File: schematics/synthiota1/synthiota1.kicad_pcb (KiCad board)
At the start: 2 copper layers, 177.8 x 114.3 mm, 111 parts, among them IC1 H11L1, J1 PJ-320A-4P DIP, J2 PJ-320A-4P DIP, SW1 SW_Push, SW2 SW_Push, SW3 SW_Push, U1 Pico, U2 74HC4051, U3 MPR121QR2, U4 MPR121QR2

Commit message: pcb cleanup
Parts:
- moved C25 8.53 mm to (179.9, 49.6)
- moved C26 8.53 mm to (163.1, 49.6)
- moved LED25 8.53 mm to (140.9, 48.9)
- moved LED26 8.53 mm to (155.9, 48.9)
- moved LED27 8.53 mm to (170.9, 48.9)
- moved SW1 8.53 mm to (167.7, 39.6)
- moved SW2 8.53 mm to (137.7, 39.6)
- moved SW3 8.53 mm to (152.7, 39.6)
- moved C27 8.52 mm to (148.3, 49.6)
- moved SLIDER2 1.13 mm to (132.5, 77.9)
- moved SLIDER1 0.87 mm to (30.5, 78.1)
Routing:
- net +VLED: track 947.3 -> 937.9 mm
- net /SWA: track 124.4 -> 132.9 mm
- net Net-(LED24-DOUT): track 86.4 -> 78.2 mm
- net /SWB: track 104.2 -> 112.3 mm
- net /SWC: track 116.1 -> 124.1 mm
- net Net-(U4-ELE2): track 78.9 -> 81.0 mm
- net Net-(U4-ELE0): track 30.7 -> 32.5 mm
- net Net-(U4-ELE1): track 56.2 -> 54.9 mm
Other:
- board text added: "PJ320A"
- board text added: "prototype"

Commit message: pcb cleanup
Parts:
- added C33: 100n, Capacitor_SMD:C_0603_1608Metric, B.Cu at (97.4, 43.0)
- added MODULE2: ~, todbot_eagle2023:I2S_PCM_5100_SOUNDCARD, F.Cu at (157.2, 33.5)
- MODULE1: value ~ -> Pico; footprint todbot_eagle2023:I2S_PCM_5100_SOUNDCARD -> todbot_RPI_Pico:RPi_Pico_SMD_TH
- U1: value Pico -> H11L1; footprint todbot_RPI_Pico:RPi_Pico_SMD_TH -> easyeda2kicad:SMD-6_L7.3-W6.5-P2.54-LS10.2-BL; moved to B.Cu
- moved MODULE1 113.0 mm to (44.2, 33.3), turned to 90 degrees
- moved U1 62.3 mm to (106.4, 31.0), turned to -90 degrees
- moved C25 32.0 mm to (147.9, 49.6)
- moved C27 31.6 mm to (179.9, 49.6)
- moved R23 2.30 mm to (27.9, 69.8)
- moved R22 2.20 mm to (23.4, 69.8)
- renumbered C100 to C28, C104 to C29, C103 to C30, C101 to C31, C102 to C32, D100 to D1, R17 to R1, R18 to R2, R20 to R3, R19 to R4, R24 to R5, R21 to R6, IC1 to U1
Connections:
- D1 pad 1: Net-(D100-K) -> Net-(D1-K)
- D1 pad 2: Net-(D100-A) -> Net-(D1-A)
- J2 pad D: Net-(D100-A) -> Net-(D1-A)
- MODULE1 pad 3: unconnected-(MODULE1-Pad3) -> GND
- MODULE1 pad 4: unconnected-(MODULE1-Pad4) -> /SDA
- MODULE1 pad 5: unconnected-(MODULE1-Pad5) -> /SCL
- R3 pad 2: Net-(D100-K) -> Net-(D1-K)
- U1 pad 1: Net-(D100-K) -> Net-(D1-K)
- U1 pad 2: Net-(D100-A) -> Net-(D1-A)
- U1 pad 3: unconnected-(IC1-Pad3) -> unconnected-(U1-Pad3)
- U1 pad 1: unconnected-(U1-GPIO0-Pad1) -> Net-(D1-K)
- U1 pad 2: unconnected-(U1-GPIO1-Pad2)_1 -> Net-(D1-A)
- U1 pad 3: GND -> unconnected-(U1-Pad3)
- U1 pad 4: /SDA -> /MIDI_IN
- U1 pad 5: /SCL -> GND
- U1 pad 6: unconnected-(U1-GPIO4-Pad6) -> +3V3
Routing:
- net Net-(D100-A): track 31.4 -> 0.00 mm
- net Net-(D1-A): track 0.00 -> 31.4 mm
- net Net-(D100-K): track 14.7 -> 0.00 mm
- net Net-(D1-K): track 0.00 -> 14.7 mm
- net +VLED: track 937.9 -> 950.7 mm
- net /SDA: track 155.1 -> 151.8 mm
- net /SCL: track 153.9 -> 151.0 mm
- net Net-(LED16-DOUT): track 231.3 -> 230.2 mm
- net +3V3: track 453.2 -> 453.8 mm
- net /LEDDAT: track 130.3 -> 130.8 mm
- net GND: vias 3 -> 5
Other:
- board text added: "3V3"
- board text added: "VLED"
- board text added: "VSYS"

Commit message: pcb tweaks
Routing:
- net Net-(LED16-DOUT): track 230.2 -> 229.3 mm
- net +VLED: track 950.7 -> 949.8 mm
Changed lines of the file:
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@@
 	)
 	(via
-		(at 25.6 83.6)
+		(at 150.325 49.6)
 		(size 0.6)
 		(drill 0.3)
 		(layers "F.Cu" "B.Cu")
-		(free yes)
 		(net 3)
 	)
 	(via
-		(at 150.325 49.6)
+		(at 23.4 81.4)
 		(size 0.6)
 		(drill 0.3)
 		(layers "F.Cu" "B.Cu")
+		(free yes)
 		(net 3)
 	)
 	(via
-		(at 23.4 81.4)
+		(at 25 84)
 		(size 0.6)
 		(drill 0.3)
@@
 	)
 	(segment
-		(start 22.4 105.2)
-		(end 18.162 100.962)
-		(width 0.5)
-		(layer "B.Cu")
-		(net 57)
-	)
-	(segment
 		(start 175.925 49.65)
 		(end 179.1 49.65)
@@
 	)
 	(segment
-		(start 27.56 30.16)
-		(end 27.56 27.846)
-		(width 0.5)
-		(layer "B.Cu")
-		(net 57)
-	)
-	(segment
 		(start 139.125 105.125)
 		(end 139.125 97.25)
@@
 	)
 	(segment
-		(start 34.65 36.95)
-		(end 34.65 32.65)
-		(width 0.5)
-		(layer "B.Cu")
-		(net 57)
-	)
-	(segment
 		(start 145.725 49.6)
 		(end 145.675 49.65)
@@
 	)
 	(segment
+		(start 23.8 105.2)
+		(end 18.162 99.562)
+		(width 0.5)
+		(layer "B.Cu")
+		(net 57)
+	)
+	(segment
 		(start 145.725 49.6)
 		(end 147.55 49.6)
@@
 	)
 	(segment
+		(start 34.65 36.95)
+		(end 34.65 32.65)
+		(width 0.5)
+		(layer "B.Cu")
+		(net 57)
+	)
+	(segment
 		(start 184.375 74.15)
 		(end 184.625 74.4)
@@
 	)
 	(segment
+		(start 33.086 38.514)
+		(end 34.65 36.95)
+		(width 0.5)
+		(layer "B.Cu")
+		(net 57)
+	)
+	(segment
 		(start 79.125 117.25)
 		(end 82.375 117.25)
@@
 	)
 	(segment
-		(start 18.162 100.962)
+		(start 18.162 99.562)
 		(end 18.162 40.292)
 		(width 0.5)
@@
 	)
 	(segment
-		(start 33 31)
-		(end 28.4 31)
-		(width 0.5)
-		(layer "B.Cu")
-		(net 57)
-	)
-	(segment
 		(start 79.125 104.2)
 		(end 79.125 97.25)
@@
 	)
 	(segment
+		(start 34.65 32.65)
+		(end 33 31)
+		(width 0.5)
+		(layer "B.Cu")
+		(net 57)
+	)
+	(segment
 		(start 162.375 117.25)
 		(end 163.025 117.9)
@@
 	)
 	(segment
+		(start 18.162 40.292)
+		(end 19.94 38.514)
+		(width 0.5)
+		(layer "B.Cu")
+		(net 57)
+	)
+	(segment
 		(start 160.125 76.525)
 		(end 160.2 76.6)
@@
 	)
 	(segment
-		(start 18.162 40.292)
-		(end 19.94 38.514)
-		(width 0.5)
+		(start 159.125 105.125)
+		(end 159.125 97.25)
+		(width 0.3048)
 		(layer "B.Cu")
 		(net 57)
 	)
 	(segment
-		(start 34.65 32.65)
-		(end 33 31)
+		(start 28.4 31)
+		(end 27.56 30.16)
 		(width 0.5)
 		(layer "B.Cu")
@@
 	)
 	(segment
-		(start 159.125 105.125)
-		(end 159.125 97.25)
-		(width 0.3048)
-		(layer "B.Cu")
-		(net 57)
-	)
-	(segment
 		(start 23.8 105.2)
 		(end 23.8 122.8)
@@
 	)
 	(segment
-		(start 19.94 38.514)
-		(end 33.086 38.514)
-		(width 0.5)
-		(layer "B.Cu")
-		(net 57)
-	)
-	(segment
 		(start 99.9 104.3)
 		(end 99.125 103.525)
@@
 	)
 	(segment
-		(start 28.4 31)
-		(end 27.56 30.16)
-		(width 0.5)
-		(layer "B.Cu")
-		(net 57)
-	)
-	(segment
 		(start 159.125 97.25)
 		(end 162.375 97.25)
@@
 	)
 	(segment
+		(start 27.56 30.16)
+		(end 27.56 27.846)
+		(width 0.5)
+		(layer "B.Cu")
+		(net 57)
+	)
+	(segment
 		(start 163.025 125.625)
 		(end 163.2 125.8)
@@
 	)
 	(segment
-		(start 33.086 38.514)
-		(end 34.65 36.95)
+		(start 19.94 38.514)
+		(end 33.086 38.514)
 		(width 0.5)
 		(layer "B.Cu")
@@
 	)
 	(segment
-		(start 23.8 105.2)
-		(end 22.4 105.2)
+		(start 33 31)
+		(end 28.4 31)
 		(width 0.5)
 		(layer "B.Cu")
@@
 	)
 	(segment
-		(start 29.2 74.15)
-		(end 29.05 74.15)
+		(start 21.6 81.6)
+		(end 21.6 106.8)
 		(width 0.3048)
 		(layer "F.Cu")
@@
 	)
 	(segment
-		(start 21 82.2)
-		(end 21 107)
+		(start 21.6 106.8)
+		(end 22.8 108)
 		(width 0.3048)
 		(layer "F.Cu")
@@
 	)
 	(segment
-		(start 22 108)
-		(end 188.8 108)
+		(start 29.2 74.15)
+		(end 29.05 74.15)
 		(width 0.3048)
 		(layer "F.Cu")
@@
 	)
 	(segment
-		(start 21 107)
-		(end 22 108)
+		(start 29.05 74.15)
+		(end 21.6 81.6)
 		(width 0.3048)
 		(layer "F.Cu")
@@
 	)
 	(segment
-		(start 29.05 74.15)
-		(end 21 82.2)
+		(start 22.8 108)
+		(end 188.8 108)
 		(width 0.3048)
 		(layer "F.Cu")

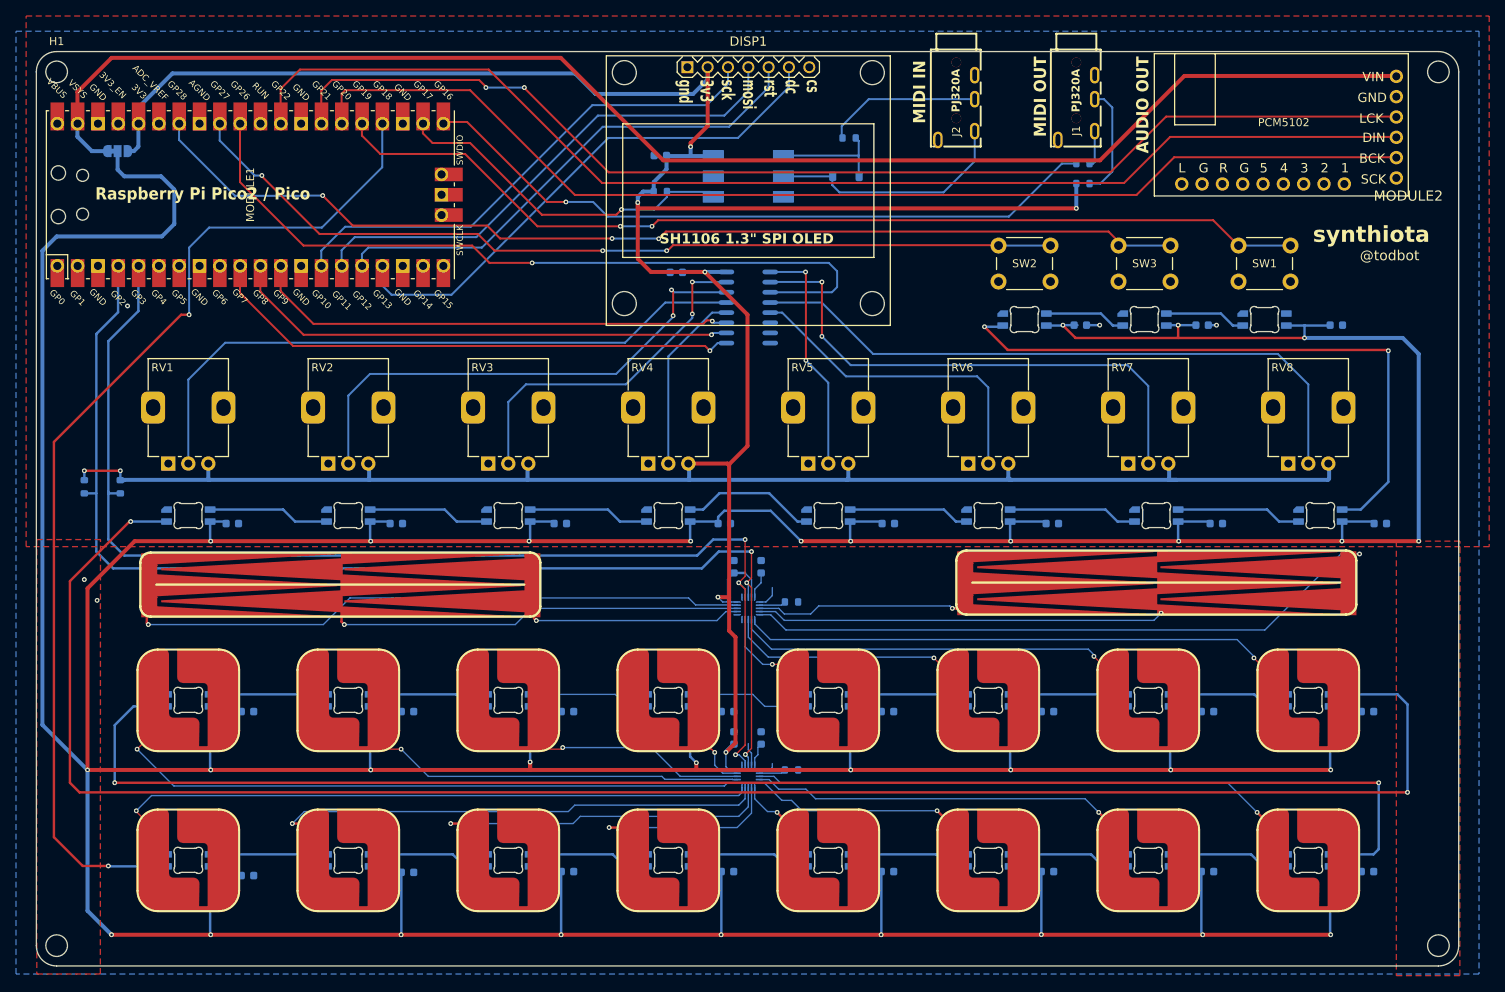
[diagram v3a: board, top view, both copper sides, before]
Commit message: lcsc part nums for everything because jlc sucks now, pcb cleanup
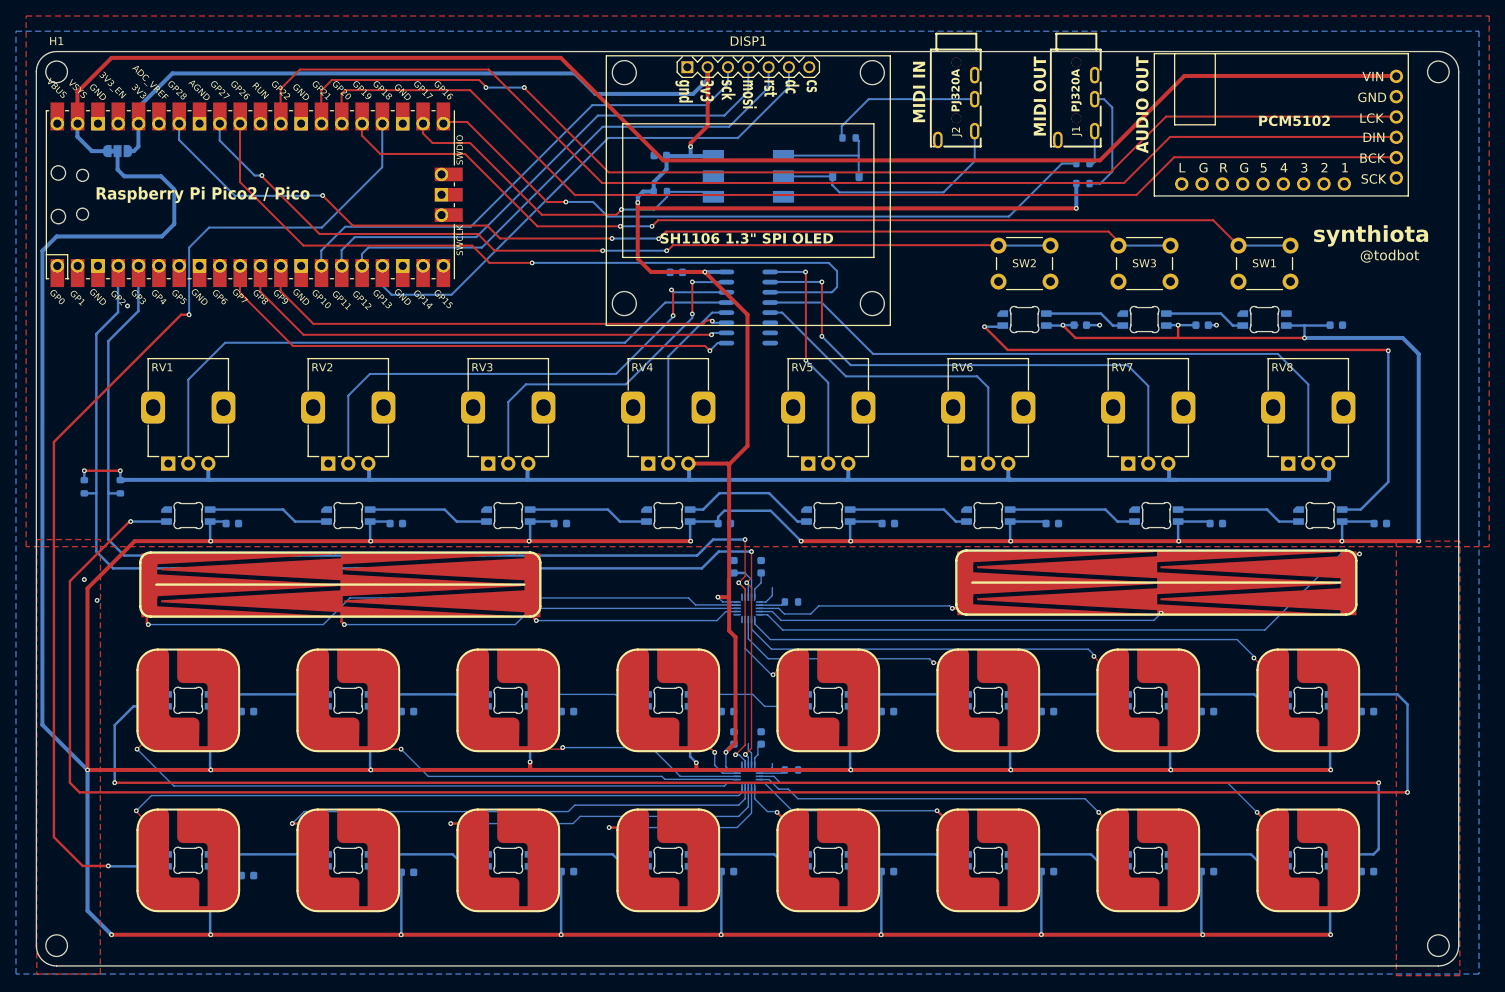
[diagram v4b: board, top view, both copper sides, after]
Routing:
- net Net-(TP13-A): track 19.0 -> 19.9 mm

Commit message: added up/dn buttons! and more pcb tweaks
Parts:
- added TP17: Capacitive_Button, todbot_stuff:Pad-CapTouch-8mm-roundrect, F.Cu at (95.4, 82.4)
- added TP18: Capacitive_Button, todbot_stuff:Pad-CapTouch-8mm-roundrect, F.Cu at (117.4, 82.4)
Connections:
- U4 pad 15: unconnected-(U4-LED3/ELE7-Pad15) -> Net-(TP18-A)
- U4 pad 16: unconnected-(U4-LED4/ELE8-Pad16) -> Net-(TP17-A)
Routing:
- net Net-(TP18-A): track 0.00 -> 26.8 mm, vias 0 -> 1
- net Net-(TP17-A): track 0.00 -> 18.5 mm, vias 0 -> 1
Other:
- board text added: "4051"
- board text added: "H11L1"
- board text added: "MPR121"
- board text added: "TRRS stereo"
- board text added: "edit"
- board text added: "mode"
- board text added: "play"
- board text added: "vin gnd lck din bck sck"
- board text added: "↑"
- board text added: "↓"

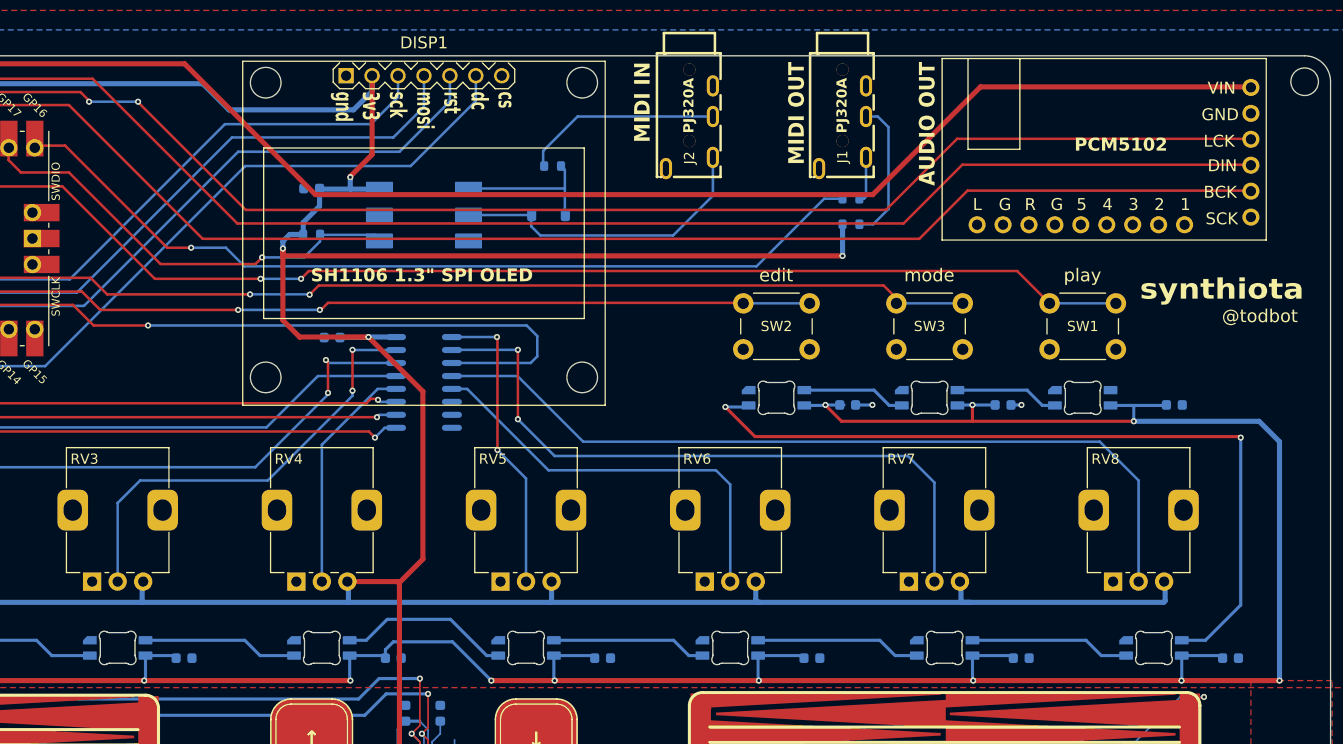
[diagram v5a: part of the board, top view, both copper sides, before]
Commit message: rotary encoder instead
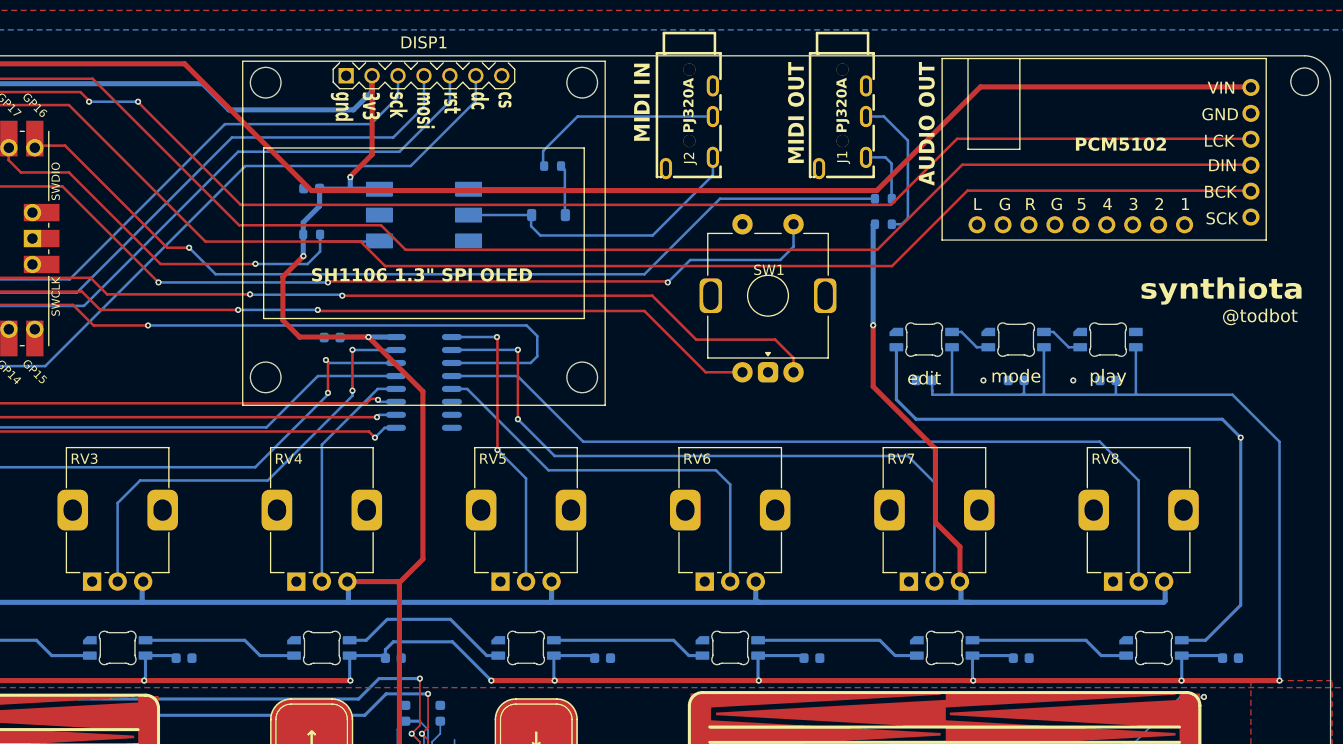
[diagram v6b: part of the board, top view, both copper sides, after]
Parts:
- removed SW2, SW3: SW_Push, Button_Switch_THT:SW_PUSH_6mm_H4.3mm
- SW1: value SW_Push -> RotaryEncoder_Switch_MP; footprint Button_Switch_THT:SW_PUSH_6mm_H4.3mm -> PCM_marbastlib-various:ROT_Alps_EC11E-Switch
- moved SW1 27.6 mm to (140.1, 38.9)
- moved LED25 15.6 mm to (155.4, 43.2)
- moved LED26 10.2 mm to (164.4, 43.2)
- moved C25 7.87 mm to (155.4, 47.2), turned to 180 degrees
- moved C27 6.93 mm to (173.4, 47.2), turned to 180 degrees
- moved LED27 6.21 mm to (173.4, 43.2)
- moved R1 3.18 mm to (151.4, 29.4)
- moved R2 3.18 mm to (151.4, 31.9)
- moved C26 2.72 mm to (164.4, 47.2), turned to 180 degrees
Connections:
- MODULE1 pad 32: /SWB -> /SWA
- MODULE1 pad 34: /SWA -> /SWB
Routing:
- net /SWC: track 124.1 -> 94.8 mm, vias 2 -> 3
- net /SWA: track 132.9 -> 107.9 mm
- net +3V3: track 453.8 -> 433.1 mm
- net Net-(LED24-DOUT): track 78.2 -> 64.1 mm, vias 2 -> 1
- net +VLED: track 949.8 -> 943.0 mm, vias 31 -> 28
- net /SWB: track 112.3 -> 118.7 mm
- net Net-(LED26-DOUT): track 9.67 -> 4.17 mm
- net Net-(LED25-DOUT): track 9.67 -> 4.17 mm
- net /MIDI_OUT: track 86.8 -> 90.6 mm
- net GND: track 10.3 -> 8.06 mm
- net /I2S_BCK: track 142.9 -> 145.1 mm
- net /I2S_DATA: track 152.9 -> 155.0 mm
- net Net-(J1-PadD): track 4.58 -> 6.21 mm
- net /MIDI_IN: track 43.9 -> 45.1 mm
- net Net-(D1-A): track 31.4 -> 30.2 mm
